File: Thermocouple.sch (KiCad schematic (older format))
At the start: 22 parts, among them P2 CONN_2, P3 CONN_3X2, U10 LMT84, U11 OPA4170, U9 MCP3901

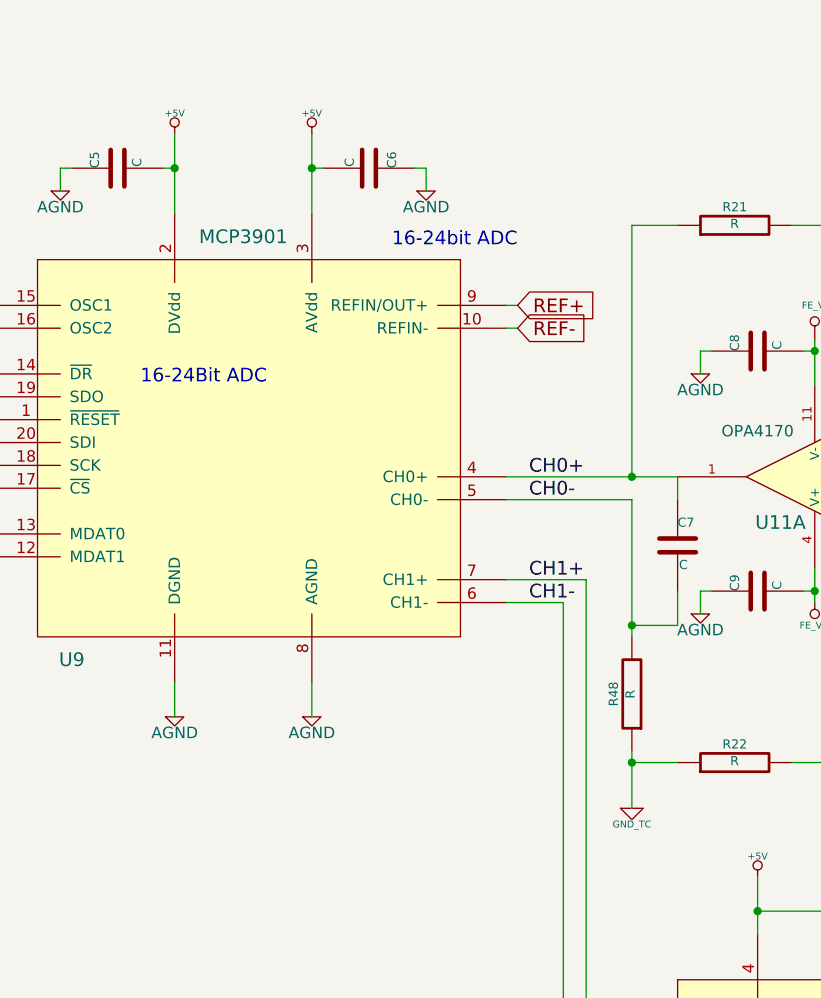
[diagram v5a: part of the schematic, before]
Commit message: Fan and TC module layout
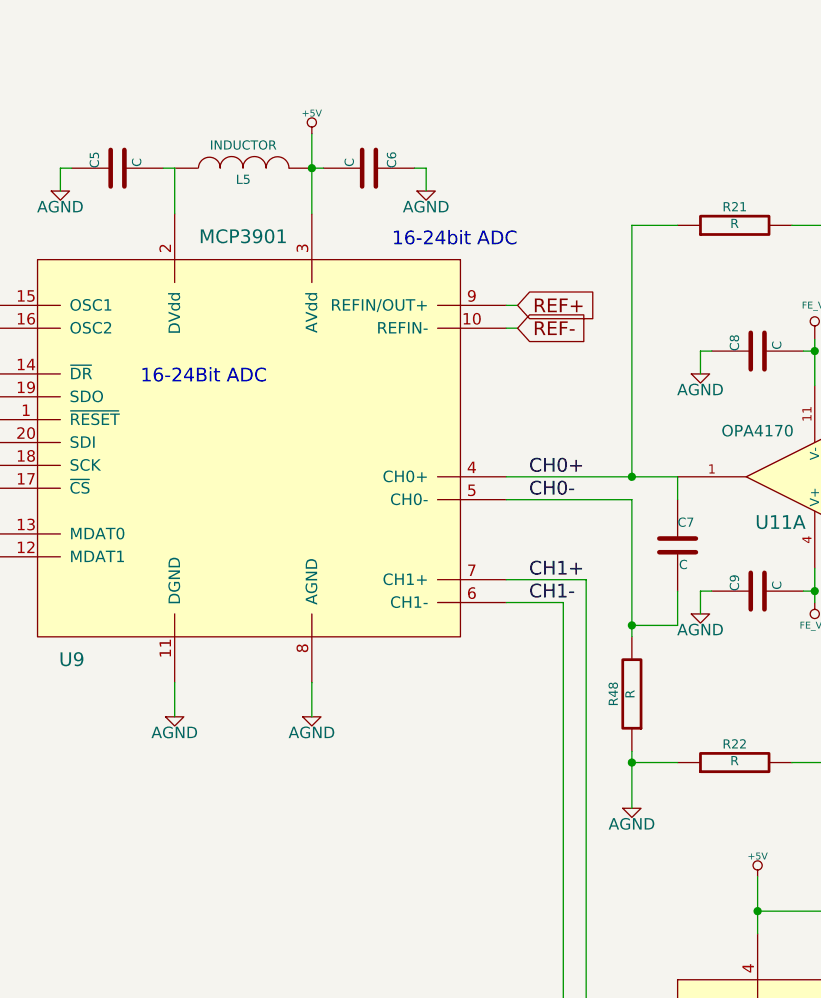
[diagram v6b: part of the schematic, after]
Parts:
- added L5: INDUCTOR, symbol INDUCTOR
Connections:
- net GND_TC is gone; now on net AGND: R22.1, R48.1
- net +5V: now also L5.2; no longer C5.2, U9.2 (DVdd)
- new net: C5.2, L5.1, U9.2 (DVdd)
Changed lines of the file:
@@
 $EndComp
 $Comp
-L +5V #PWR044
+L +5V #PWR59
 U 1 1 530546E7
 P 5050 4750
-F 0 "#PWR044" H 5050 4840 20  0001 C CNN
+F 0 "#PWR59" H 5050 4840 20  0001 C CNN
 F 1 "+5V" H 5050 4840 30  0000 C CNN
 F 2 "" H 5050 4750 60  0000 C CNN
@@
 $EndComp
 $Comp
-L +5V #PWR045
+L +5V #PWR52
 U 1 1 53054B2C
 P 3100 1500
-F 0 "#PWR045" H 3100 1590 20  0001 C CNN
+F 0 "#PWR52" H 3100 1590 20  0001 C CNN
 F 1 "+5V" H 3100 1590 30  0000 C CNN
 F 2 "" H 3100 1500 60  0000 C CNN
@@
 $EndComp
 $Comp
-L +5V #PWR046
-U 1 1 53055345
-P 2500 1500
-F 0 "#PWR046" H 2500 1590 20  0001 C CNN
-F 1 "+5V" H 2500 1590 30  0000 C CNN
-F 2 "" H 2500 1500 60  0000 C CNN
-F 3 "" H 2500 1500 60  0000 C CNN
-	1    2500 1500
-	-1   0    0    -1
-$EndComp
-$Comp
 L C C5
 U 1 1 5305534C
@@
 Wire Wire Line
 	2050 1650 2000 1650
-Connection ~ 2500 1650
-Wire Wire Line
-	2450 1650 2500 1650
 Wire Wire Line
 	2000 1650 2000 1750
-Wire Wire Line
-	2500 1500 2500 1850
 Wire Wire Line
 	2500 4050 2500 3900
@@
 	1050 3050 1700 3050
 $Comp
-L FE_V+ #PWR047
+L FE_V+ #PWR65
 U 1 1 530BD56D
 P 7800 4750
-F 0 "#PWR047" H 7800 4850 30  0001 C CNN
+F 0 "#PWR65" H 7800 4850 30  0001 C CNN
 F 1 "FE_V+" H 7800 4850 30  0000 C CNN
 F 2 "" H 7800 4750 60  0000 C CNN
@@
 $EndComp
 $Comp
-L FE_V+ #PWR048
+L FE_V+ #PWR61
 U 1 1 530BD573
 P 5300 3550
-F 0 "#PWR048" H 5300 3650 30  0001 C CNN
+F 0 "#PWR61" H 5300 3650 30  0001 C CNN
 F 1 "FE_V+" H 5300 3650 30  0000 C CNN
 F 2 "" H 5300 3550 60  0000 C CNN
@@
 $EndComp
 $Comp
-L FE_V- #PWR61
+L FE_V- #PWR60
 U 1 1 530BD604
 P 5300 2400
-F 0 "#PWR61" H 5300 2600 40  0001 C CNN
+F 0 "#PWR60" H 5300 2600 40  0001 C CNN
 F 1 "FE_V-" H 5300 2550 30  0000 C CNN
 F 2 "" H 5300 2400 60  0000 C CNN
@@
 $EndComp
 $Comp
-L FE_V+ #PWR049
+L FE_V+ #PWR62
 U 1 1 530BD635
 P 7800 1400
-F 0 "#PWR049" H 7800 1500 30  0001 C CNN
+F 0 "#PWR62" H 7800 1500 30  0001 C CNN
 F 1 "FE_V+" H 7800 1500 30  0000 C CNN
 F 2 "" H 7800 1400 60  0000 C CNN
@@
 $EndComp
 $Comp
-L FE_V- #PWR64
+L FE_V- #PWR63
 U 1 1 530BD640
 P 7800 2400
-F 0 "#PWR64" H 7800 2600 40  0001 C CNN
+F 0 "#PWR63" H 7800 2600 40  0001 C CNN
 F 1 "FE_V-" H 7800 2550 30  0000 C CNN
 F 2 "" H 7800 2400 60  0000 C CNN
@@
 $EndComp
 $Comp
-L FE_V- #PWR65
+L FE_V- #PWR64
 U 1 1 530BD64B
 P 7800 3750
-F 0 "#PWR65" H 7800 3950 40  0001 C CNN
+F 0 "#PWR64" H 7800 3950 40  0001 C CNN
 F 1 "FE_V-" H 7800 3900 30  0000 C CNN
 F 2 "" H 7800 3750 60  0000 C CNN
@@
 	1    0    0    -1
 $EndComp
-$Comp
-L GND_TC #PWR050
-U 1 1 531521C2
-P 4500 4450
-F 0 "#PWR050" H 4500 4450 30  0001 C CNN
-F 1 "GND_TC" H 4500 4380 30  0000 C CNN
-F 2 "" H 4500 4450 60  0000 C CNN
-F 3 "" H 4500 4450 60  0000 C CNN
-	1    4500 4450
-	1    0    0    -1
-$EndComp
 Connection ~ 4200 6300
 $Comp
-L AGND #PWR051
+L AGND #PWR50
 U 1 1 531630FA
 P 2000 1750
-F 0 "#PWR051" H 2000 1750 40  0001 C CNN
+F 0 "#PWR50" H 2000 1750 40  0001 C CNN
 F 1 "AGND" H 2000 1680 50  0000 C CNN
 F 2 "" H 2000 1750 60  0000 C CNN
@@
 $EndComp
 $Comp
-L AGND #PWR052
+L AGND #PWR54
 U 1 1 53163116
 P 3600 1750
-F 0 "#PWR052" H 3600 1750 40  0001 C CNN
+F 0 "#PWR54" H 3600 1750 40  0001 C CNN
 F 1 "AGND" H 3600 1680 50  0000 C CNN
 F 2 "" H 3600 1750 60  0000 C CNN
@@
 $EndComp
 $Comp
-L AGND #PWR053
+L AGND #PWR51
 U 1 1 5316312B
 P 2500 4050
-F 0 "#PWR053" H 2500 4050 40  0001 C CNN
+F 0 "#PWR51" H 2500 4050 40  0001 C CNN
 F 1 "AGND" H 2500 3980 50  0000 C CNN
 F 2 "" H 2500 4050 60  0000 C CNN
@@
 $EndComp
 $Comp
-L AGND #PWR054
+L AGND #PWR53
 U 1 1 53163136
 P 3100 4050
-F 0 "#PWR054" H 3100 4050 40  0001 C CNN
+F 0 "#PWR53" H 3100 4050 40  0001 C CNN
 F 1 "AGND" H 3100 3980 50  0000 C CNN
 F 2 "" H 3100 4050 60  0000 C CNN
@@
 $EndComp
 $Comp
-L AGND #PWR055
+L AGND #PWR55
 U 1 1 53163155
 P 4200 6450
-F 0 "#PWR055" H 4200 6450 40  0001 C CNN
+F 0 "#PWR55" H 4200 6450 40  0001 C CNN
 F 1 "AGND" H 4200 6380 50  0000 C CNN
 F 2 "" H 4200 6450 60  0000 C CNN
@@
 $EndComp
 $Comp
-L AGND #PWR056
+L AGND #PWR57
 U 1 1 5316316A
 P 4800 2550
-F 0 "#PWR056" H 4800 2550 40  0001 C CNN
+F 0 "#PWR57" H 4800 2550 40  0001 C CNN
 F 1 "AGND" H 4800 2480 50  0000 C CNN
 F 2 "" H 4800 2550 60  0000 C CNN
@@
 $EndComp
 $Comp
-L AGND #PWR057
+L AGND #PWR58
 U 1 1 53163175
 P 4800 3600
-F 0 "#PWR057" H 4800 3600 40  0001 C CNN
+F 0 "#PWR58" H 4800 3600 40  0001 C CNN
 F 1 "AGND" H 4800 3530 50  0000 C CNN
 F 2 "" H 4800 3600 60  0000 C CNN
@@
 	1    0    0    -1
 $EndComp
+$Comp
+L AGND #PWR56
+U 1 1 531E51B9
+P 4500 4450
+F 0 "#PWR56" H 4500 4450 40  0001 C CNN
+F 1 "AGND" H 4500 4380 50  0000 C CNN
+F 2 "" H 4500 4450 60  0000 C CNN
+F 3 "" H 4500 4450 60  0000 C CNN
+	1    4500 4450
+	1    0    0    -1
+$EndComp
+$Comp
+L INDUCTOR L5
+U 1 1 531E57F7
+P 2800 1650
+F 0 "L5" V 2750 1650 40  0000 C CNN
+F 1 "INDUCTOR" V 2900 1650 40  0000 C CNN
+F 2 "" H 2800 1650 60  0000 C CNN
+F 3 "" H 2800 1650 60  0000 C CNN
+	1    2800 1650
+	0    -1   -1   0
+$EndComp
+Wire Wire Line
+	2500 1650 2450 1650
+Wire Wire Line
+	2500 1650 2500 1850
 $EndSCHEMATC
